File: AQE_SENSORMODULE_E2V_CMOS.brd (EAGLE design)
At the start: 100 x 80 mm, 14 parts, among them IC1 TINY24/44/84-SSU, J1 440055-4, J2 AVR_SPI_PRG_6NS

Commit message: initial layout
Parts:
- removed U$1: ABLS, wicked-device:ABLS
- removed U$2: LD1117XX, wicked-device:DPAK
- added U1: LD1117XX, wicked-device:DPAK
- added XT1: ABLS, wicked-device:ABLS
- moved J2 103.3 mm to (19.1, 5.08), turned to 180 degrees
- moved R4 96.8 mm to (11.7, 18.9)
- moved R3 93.8 mm to (20.1, 24.6), turned to 90 degrees
- moved R2 92.9 mm to (22.9, 24.6), turned to 90 degrees
- moved U$4 87.3 mm to (20.8, 32.5), turned to 90 degrees
- moved J1 83.0 mm to (10.2, 7.62), turned to 90 degrees
- moved C2 75.0 mm to (27.7, 26.4), turned to 90 degrees
- moved C4 74.1 mm to (12.6, 26.4)
- moved C1 65.6 mm to (27.7, 6.10), turned to 270 degrees
- moved C3 59.7 mm to (5.84, 15.7)
- moved R1 55.1 mm to (19.1, 10.2)
- moved IC1 47.8 mm to (19.1, 17.8), turned to 90 degrees
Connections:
- net 1.8V: now also U1.4; no longer U$2.4
- net GND: now also U1.1; no longer U$2.1
- net VCC: now also U1.3; no longer U$2.3
- net XTAL1: now also XT1.2; no longer U$1.2
- net XTAL2: now also XT1.1; no longer U$1.1
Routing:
- net ADC5: track 0.00 -> 69.3 mm
- net VCC: track 0.00 -> 49.4 mm
- net 1.8V: track 0.00 -> 43.7 mm
- net SDA: track 0.00 -> 37.1 mm
- net ADC1: track 0.00 -> 34.6 mm
- net SCL: track 0.00 -> 29.4 mm, vias 0 -> 1
- net GND: track 0.00 -> 15.5 mm, vias 0 -> 6
- net XTAL1: track 0.00 -> 15.1 mm
- net /RESET: track 0.00 -> 15.1 mm
- net XTAL2: track 0.00 -> 14.3 mm
- net N$3: track 0.00 -> 5.63 mm
- added copper zone on layer 16, net GND
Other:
- board size 100 x 80 mm -> 31.2 x 39.1 mm
- board text added: "1"
- board text added: "C4"

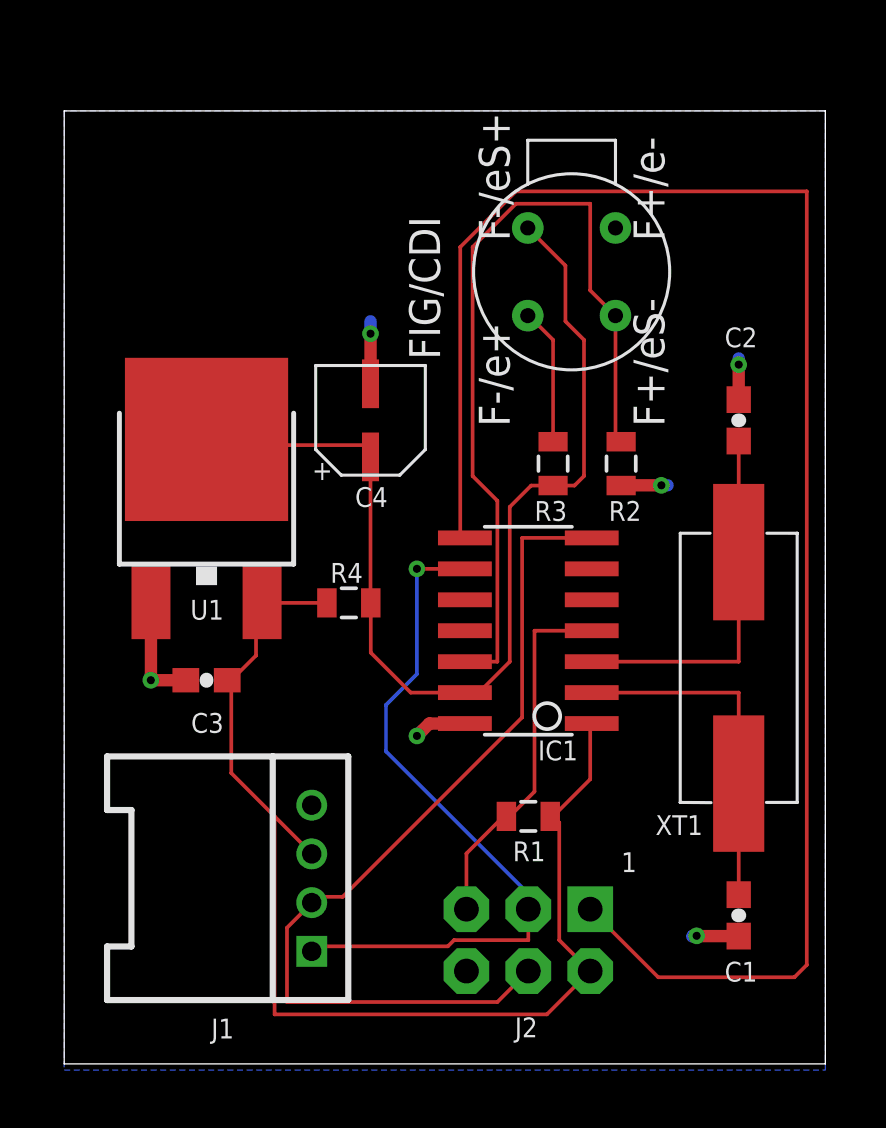
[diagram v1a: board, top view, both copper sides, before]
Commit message: aded MAC chip, switched to lm317 adjustable regulator, and re-routed the board by hand
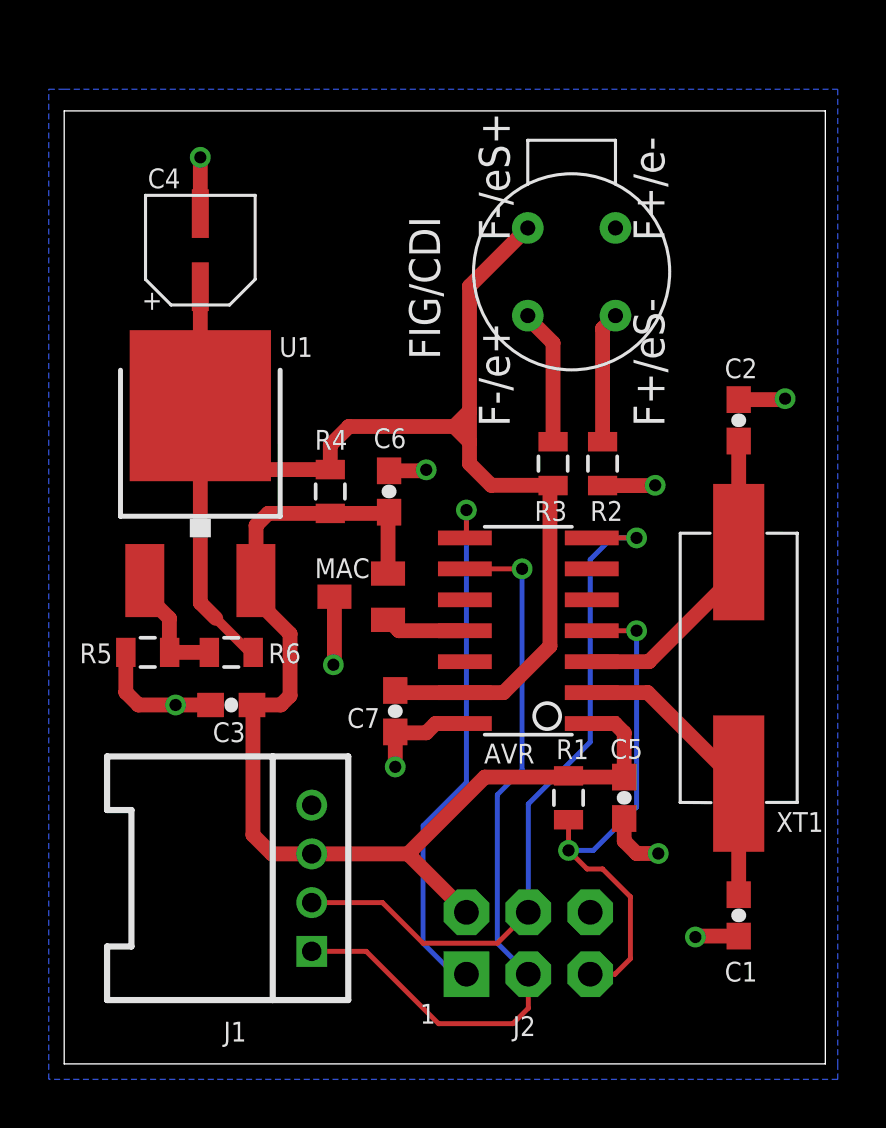
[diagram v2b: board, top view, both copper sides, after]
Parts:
- added C5, C6, C7: 0.1uF, SparkFun:0603-CAP
- added MAC: 11AA02E48, nanode:SOT23
- added R5: 150Ohm, SparkFun:0805
- added R6: 330Ohm, SparkFun:0805
- C1, C2: value (none) -> 22pF
- C3: value (none) -> 0.1uF
- C4: value EEE-1EA100WR -> 10uF
- U1: value LD1117XX -> V_REG_317DPACK; device wicked-device:DPAK -> SparkFun:V-REG_DPACK
- moved C4 9.88 mm to (5.59, 33.4)
- moved R4 4.64 mm to (10.9, 23.5), turned to 90 degrees
- moved U1 2.81 mm to (5.59, 24.6)
- moved R1 1.82 mm to (20.7, 10.9), turned to 90 degrees
- moved C3 1.44 mm to (6.86, 14.7)
- moved R2 0.76 mm to (22.1, 24.6)
- moved J2 0.13 mm to (19.1, 4.95), turned to 0 degrees
- renumbered IC1 to AVR
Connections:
- removed net ADC2: AVR.11
- new net ADC6: R2.2, U$4.FIGV+/E2VSIG
- new net MAC_IO: AVR.11, MAC.1
- new net N$1: R5.2, R6.1, U1.1
- net 1.8V: now also C7.1, R6.2
- net ADC1: no longer R2.2, U$4.FIGV+/E2VSIG
- net GND: now also C5.2, C6.2, C7.2, MAC.3, R5.1; no longer U1.1
- net VCC: now also C5.1, C6.1, MAC.2
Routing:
- net ADC5: track 69.3 -> 22.0 mm, vias 0 -> 1
- net ADC1: track 34.6 -> 0.00 mm
- net 1.8V: track 43.7 -> 57.8 mm
- net GND: track 15.5 -> 26.3 mm, vias 6 -> 9
- net SDA: track 37.1 -> 29.8 mm, vias 0 -> 1
- net /RESET: track 15.1 -> 21.9 mm, vias 0 -> 2
- net ADC6: track 0.00 -> 5.39 mm
- net N$1: track 0.00 -> 5.04 mm
- net MAC_IO: track 0.00 -> 3.34 mm
- net VCC: track 49.4 -> 47.1 mm
- net SCL: track 29.4 -> 31.7 mm
- net XTAL2: track 14.3 -> 12.1 mm
- net XTAL1: track 15.1 -> 13.1 mm

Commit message: added second voltage regulator circuit, modified sensor circuit to allow 'sliding-scale' ADC approach, added standoff holes
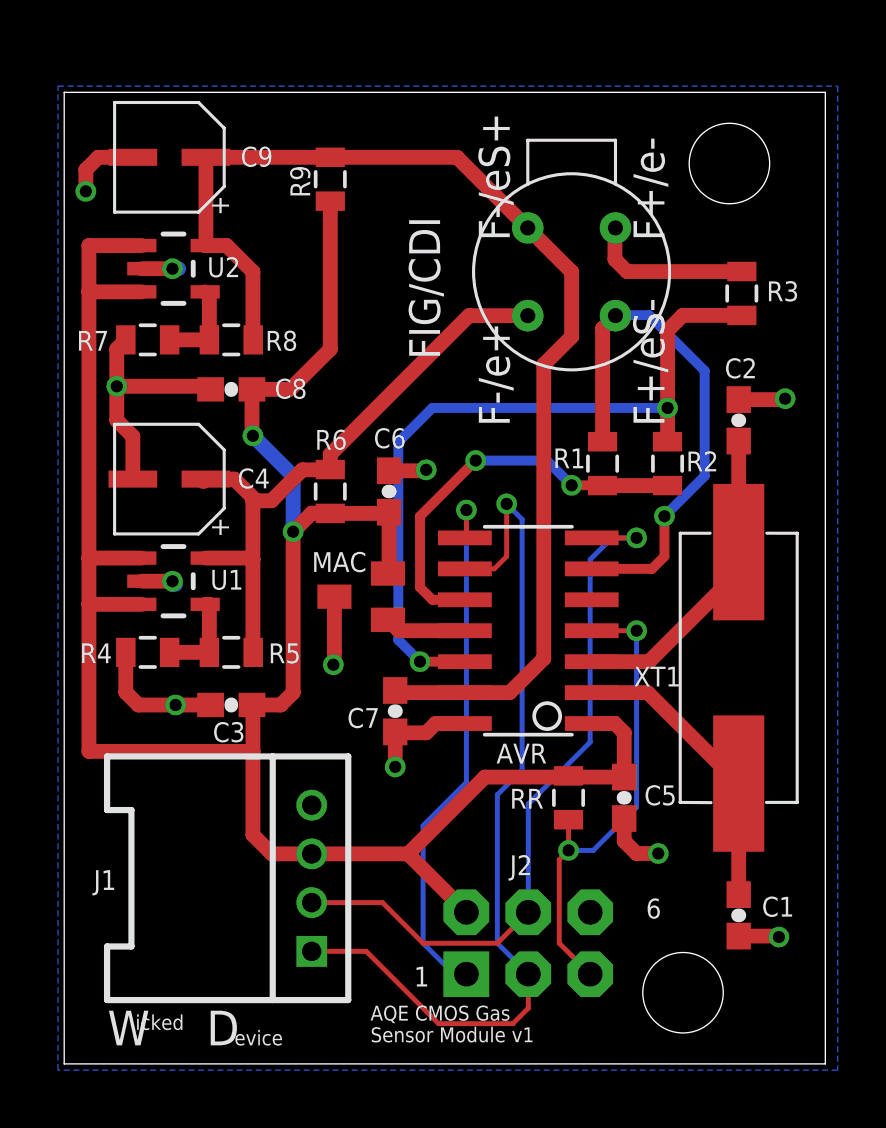
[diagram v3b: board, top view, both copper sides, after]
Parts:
- added C8: 0.1uF, SparkFun:0603-CAP
- added C9: 10uF, wicked-device:TYPE-B_ALUMINUM_CAN
- added JP1, JP2: STAND-OFF, SparkFun:STAND-OFF
- added R7: 150Ohm, SparkFun:0805
- added R8: 330Ohm, SparkFun:0805
- added R9: 0Ohm, SparkFun:0805
- added RR: 10 kOhm, SparkFun:0805
- added U2: V_REG_LDOSMD, SparkFun:SOT23-5
- R1: value 10 kOhm -> (none)
- R4: value 0Ohm -> 150Ohm
- R5: value 150Ohm -> 330Ohm
- R6: value 330Ohm -> 0Ohm
- U1: value V_REG_317DPACK -> V_REG_LDOSMD; device SparkFun:V-REG_DPACK -> SparkFun:SOT23-5
- moved R1 13.8 mm to (22.1, 24.6)
- moved R3 10.4 mm to (27.8, 31.6), turned to 270 degrees
- moved R4 9.99 mm to (3.43, 16.9), turned to 0 degrees
- moved C4 9.48 mm to (4.32, 24.0), turned to 90 degrees
- moved R6 7.75 mm to (10.9, 23.5), turned to 90 degrees
- moved U1 4.95 mm to (4.49, 19.8), turned to 270 degrees
- moved R5 3.43 mm to (6.86, 16.9)
- moved R2 2.67 mm to (24.8, 24.6), turned to 270 degrees
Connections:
- net ADC5 renamed MISO
- removed net 1.8V: AVR.13, C4.P$1, C7.1, R3.1, R4.2, R6.2, U$4.FIGG/E2VS+, U1.4
- removed net ADC1: AVR.12
- removed net ADC3: AVR.10
- removed net ADC6: R2.2, U$4.FIGV+/E2VSIG
- removed net ADC7: AVR.6
- removed net INT0: AVR.5
- removed net N$3: R3.2, U$4.FIGSIG/E2VH+
- new net /R1_SEL: AVR.10, R1.1, R2.2
- new net /R2_SEL: AVR.12, R2.1, R3.2
- new net HEATER_VCC: C4.P$1, R5.2, R6.2, U$4.FIGSIG/E2VH+, U1.5
- new net N$2: R7.2, R8.1, U2.4
- new net SENSOR: AVR.6, R1.2, U$4.FIGV+/E2VSIG
- new net SENSOR_VCC: AVR.13, C7.1, C9.P$1, R8.2, R9.2, U$4.FIGG/E2VS+, U2.5
- net /RESET: now also RR.1; no longer R1.1
- net GND: now also C8.1, C9.P$2, R3.1, R4.1, R7.1, U1.2, U2.2; no longer R2.1, R5.1
- net N$1: now also R4.2, R5.1, U1.4; no longer R5.2, R6.1, U1.1
- net VCC: now also C8.2, R6.1, R9.1, RR.2, U1.1, U2.1, U2.3; no longer R1.2, R4.1
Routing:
- net 1.8V: track 57.8 -> 0.00 mm
- net VCC: track 47.1 -> 97.3 mm, vias 0 -> 2
- net SENSOR_VCC: track 0.00 -> 48.9 mm
- net /R2_SEL: track 0.00 -> 30.7 mm, vias 0 -> 2
- net HEATER_VCC: track 0.00 -> 25.6 mm
- net SENSOR: track 0.00 -> 21.5 mm, vias 0 -> 1
- net GND: track 26.3 -> 44.7 mm, vias 9 -> 11
- net /R1_SEL: track 0.00 -> 16.5 mm, vias 0 -> 2
- net N$3: track 5.60 -> 0.00 mm
- net ADC6: track 5.39 -> 0.00 mm
- net SCL: track 31.7 -> 36.4 mm
- net N$2: track 0.00 -> 3.67 mm
- net /RESET: track 21.9 -> 19.9 mm
- net N$1: track 5.04 -> 3.82 mm
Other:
- board size 31.2 x 39.1 mm -> 31.2 x 39.9 mm
- board text added: "6"
- board text added: "AQE CMOS Gas"
- board text added: "C9"
- board text added: "D"
- board text added: "Sensor Module v1"
- board text added: "W"
- board text added: "evice"
- board text added: "icked"

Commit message: minor changes in routing and component placement for improved decoupling, more representative values for resistors, and minor changes to silk screen
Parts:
- R4, R7: value 150Ohm -> 2.4MOhm
- R5, R8: value 330Ohm -> 2.2MOhm
- moved C3 5.46 mm to (1.91, 17.0), turned to 180 degrees
- moved C8 5.35 mm to (1.91, 29.7), turned to 180 degrees
- moved R7 1.91 mm to (3.43, 27.8)
- moved R8 1.91 mm to (6.86, 27.8)
- moved R4 1.90 mm to (3.43, 15.0)
- moved R5 1.90 mm to (6.86, 15.0)
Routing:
- net GND: track 44.7 -> 37.6 mm, vias 11 -> 13
- net VCC: track 97.3 -> 102.6 mm
- net N$2: track 3.67 -> 5.58 mm
- net N$1: track 3.82 -> 5.73 mm
- net SENSOR_VCC: track 48.9 -> 50.8 mm
- net HEATER_VCC: track 25.6 -> 27.3 mm

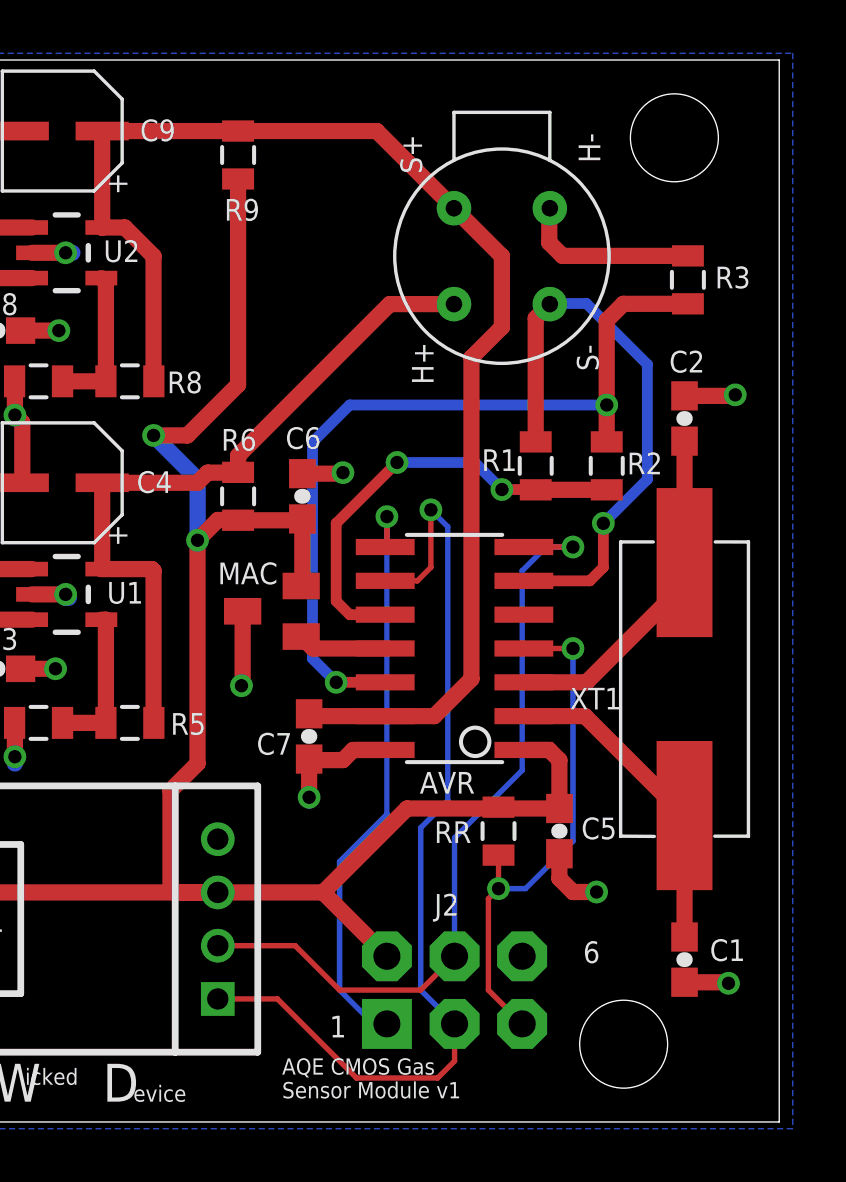
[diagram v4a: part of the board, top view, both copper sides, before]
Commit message: last changes before switching heater approach to feedback controlled and changing microcontroller
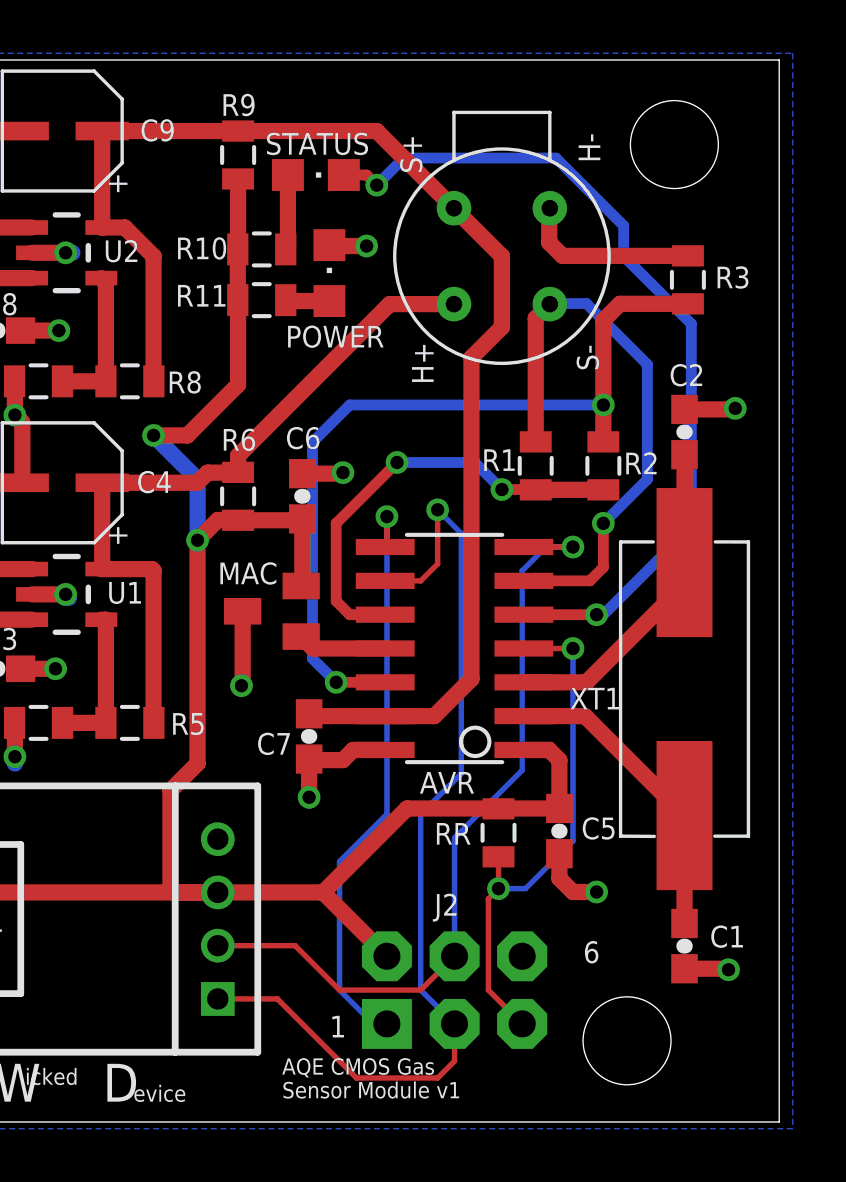
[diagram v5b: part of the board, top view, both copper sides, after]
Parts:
- added POWER: RED, adafruit:CHIPLED_0805
- added R10: 270ohm, SparkFun:0805
- added R11: 470ohm, SparkFun:0805
- added STATUS: GREEN, adafruit:CHIPLED_0805
- moved C1 0.51 mm to (27.7, 6.60)
- moved C2 0.51 mm to (27.7, 25.9)
- moved JP2 0.25 mm to (27.3, 36.7)
- moved JP1 0.18 mm to (25.5, 3.05)
- moved R2 0.13 mm to (24.6, 24.6)
- moved RR 0.06 mm to (20.7, 10.9)
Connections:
- new net N$3: POWER.A, R11.1
- new net N$4: R10.1, STATUS.A
- new net STATUS: AVR.5, STATUS.C
- net GND: now also POWER.C
- net VCC: now also R10.2, R11.2
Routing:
- net STATUS: track 0.00 -> 32.1 mm, vias 0 -> 2
- net N$4: track 0.00 -> 2.83 mm
- net N$3: track 0.00 -> 1.67 mm
- net GND: track 37.6 -> 39.2 mm, vias 13 -> 14
- net XTAL2: track 12.1 -> 11.6 mm
- net XTAL1: track 13.1 -> 12.6 mm
